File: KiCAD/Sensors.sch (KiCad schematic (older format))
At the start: 15 parts

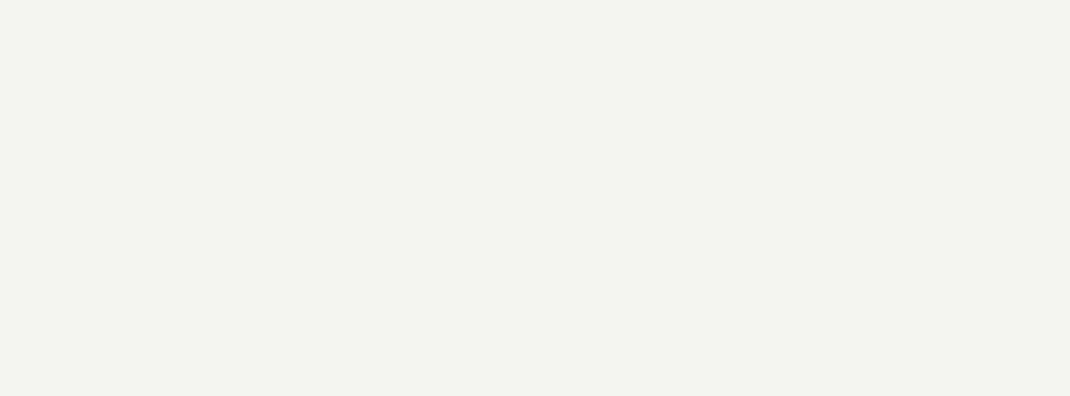
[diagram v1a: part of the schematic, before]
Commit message: Added CAN Bus Sheet
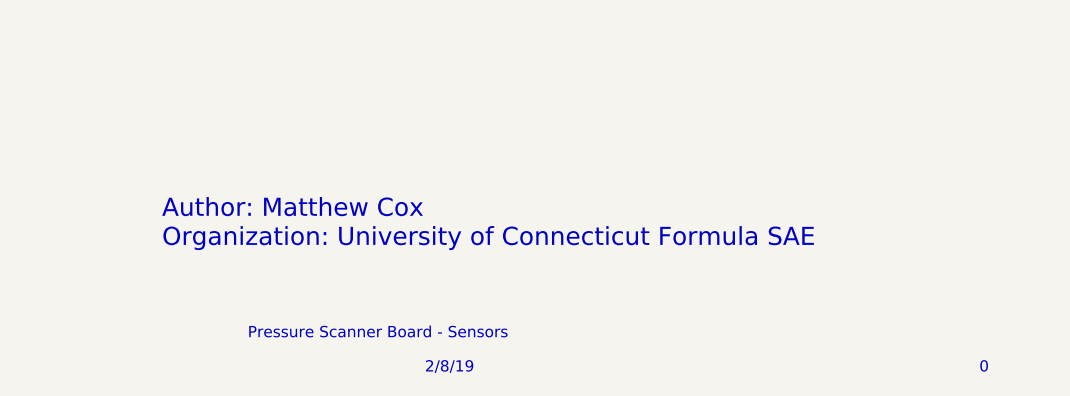
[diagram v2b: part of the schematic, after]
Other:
- note added: "0"
- note added: "2/8/19"
- note added: "Author: Matthew Cox\nOrganization: University of Connecticut Formula SAE"
- note added: "Pressure Scanner Board - Sensors"
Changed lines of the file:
@@
 LIBS:lm1117_edited
 LIBS:MF-MSMF050-2
+LIBS:mcp2515
+LIBS:mcp2551
+LIBS:cesd5v0ap
 LIBS:Pressure Scanner Board-cache
 EELAYER 25 0
@@
 $Descr A4 11693 8268
 encoding utf-8
-Sheet 3 3
+Sheet 3 4
 Title ""
 Date ""
@@
 Wire Notes Line
 	6550 1400 4325 1400
+Text Notes 7375 7500 0    49   ~ 0
+Pressure Scanner Board - Sensors
+Text Notes 8150 7650 0    49   ~ 0
+2/8/19
+Text Notes 10575 7650 0    49   ~ 0
+0
+Text Notes 7000 7100 0    79   ~ 0
+Author: Matthew Cox\nOrganization: University of Connecticut Formula SAE
 $EndSCHEMATC

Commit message: Schematic Rev 0
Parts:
- gave numbers to parts that had none: 15
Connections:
- net EOC_0: no longer names the net of U5.5 (EOC)
- net EOC_1: no longer names the net of U7.5 (EOC)
- net EOC_2: no longer names the net of U9.5 (EOC)
- net EOC_3: no longer names the net of U11.5 (EOC)
- net EOC_4: no longer names the net of U6.5 (EOC)
- net EOC_5: no longer names the net of U8.5 (EOC)
- net EOC_6: no longer names the net of U10.5 (EOC)
- net EOC_7: no longer names the net of U12.5 (EOC)
- no-connect marks 0 -> 8
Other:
- note added: "Low voltage signal -> MCU\nHigh voltage signal -> Sensor"
- moved on the sheet: Q2, Q3, R6, R7, R8, R9

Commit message: Associated sensor footprints with parts
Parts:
- U10, U11, U12, U5, U6, U7, U8, U9: footprint (none) -> DLHR-L10D-E1BD-C-NAV8:DLHR-L10D-E1BD-C-NAV8
- U4: footprint (none) -> HSCDANN015PA2A5:HSCDANN015PA2A5
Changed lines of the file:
@@
 $EndDescr
 $Comp
-L +3.3V #PWR35
+L +3.3V #PWR033
 U 1 1 5C62E178
 P 2175 1700
-F 0 "#PWR35" H 2175 1550 50  0001 C CNN
+F 0 "#PWR033" H 2175 1550 50  0001 C CNN
 F 1 "+3.3V" H 2175 1840 50  0000 C CNN
 F 2 "" H 2175 1700 50  0001 C CNN
@@
 	2175 1900 2525 1900
 $Comp
-L GND #PWR37
+L GND #PWR034
 U 1 1 5C62E1C6
 P 2425 1775
-F 0 "#PWR37" H 2425 1525 50  0001 C CNN
+F 0 "#PWR034" H 2425 1525 50  0001 C CNN
 F 1 "GND" H 2425 1625 50  0000 C CNN
 F 2 "" H 2425 1775 50  0001 C CNN
@@
 F 0 "U5" H 3075 1650 60  0000 C CNN
 F 1 "DLHR-L10D-E1BD-C-NAV8" H 3075 2300 39  0000 C CNN
-F 2 "" H 3075 1975 60  0001 C CNN
+F 2 "DLHR-L10D-E1BD-C-NAV8:DLHR-L10D-E1BD-C-NAV8" H 3075 1975 60  0001 C CNN
 F 3 "" H 3075 1975 60  0001 C CNN
 	1    3075 1975
@@
 	3825 1775 3600 1775
 $Comp
-L +3.3V #PWR43
+L +3.3V #PWR035
 U 1 1 5C62E3C1
 P 2175 2650
-F 0 "#PWR43" H 2175 2500 50  0001 C CNN
+F 0 "#PWR035" H 2175 2500 50  0001 C CNN
 F 1 "+3.3V" H 2175 2790 50  0000 C CNN
 F 2 "" H 2175 2650 50  0001 C CNN
@@
 	2175 2850 2525 2850
 $Comp
-L GND #PWR45
+L GND #PWR036
 U 1 1 5C62E3C9
 P 2425 2725
-F 0 "#PWR45" H 2425 2475 50  0001 C CNN
+F 0 "#PWR036" H 2425 2475 50  0001 C CNN
 F 1 "GND" H 2425 2575 50  0000 C CNN
 F 2 "" H 2425 2725 50  0001 C CNN
@@
 F 0 "U7" H 3075 2600 60  0000 C CNN
 F 1 "DLHR-L10D-E1BD-C-NAV8" H 3075 3250 39  0000 C CNN
-F 2 "" H 3075 2925 60  0001 C CNN
+F 2 "DLHR-L10D-E1BD-C-NAV8:DLHR-L10D-E1BD-C-NAV8" H 3075 2925 60  0001 C CNN
 F 3 "" H 3075 2925 60  0001 C CNN
 	1    3075 2925
@@
 	3825 2725 3600 2725
 $Comp
-L +3.3V #PWR47
+L +3.3V #PWR037
 U 1 1 5C62E42E
 P 2175 3600
-F 0 "#PWR47" H 2175 3450 50  0001 C CNN
+F 0 "#PWR037" H 2175 3450 50  0001 C CNN
 F 1 "+3.3V" H 2175 3740 50  0000 C CNN
 F 2 "" H 2175 3600 50  0001 C CNN
@@
 	2175 3800 2525 3800
 $Comp
-L GND #PWR49
+L GND #PWR038
 U 1 1 5C62E436
 P 2425 3675
-F 0 "#PWR49" H 2425 3425 50  0001 C CNN
+F 0 "#PWR038" H 2425 3425 50  0001 C CNN
 F 1 "GND" H 2425 3525 50  0000 C CNN
 F 2 "" H 2425 3675 50  0001 C CNN
@@
 F 0 "U9" H 3075 3550 60  0000 C CNN
 F 1 "DLHR-L10D-E1BD-C-NAV8" H 3075 4200 39  0000 C CNN
-F 2 "" H 3075 3875 60  0001 C CNN
+F 2 "DLHR-L10D-E1BD-C-NAV8:DLHR-L10D-E1BD-C-NAV8" H 3075 3875 60  0001 C CNN
 F 3 "" H 3075 3875 60  0001 C CNN
 	1    3075 3875
@@
 	3825 3675 3600 3675
 $Comp
-L +3.3V #PWR51
+L +3.3V #PWR039
 U 1 1 5C62E4AC
 P 2175 4575
-F 0 "#PWR51" H 2175 4425 50  0001 C CNN
+F 0 "#PWR039" H 2175 4425 50  0001 C CNN
 F 1 "+3.3V" H 2175 4715 50  0000 C CNN
 F 2 "" H 2175 4575 50  0001 C CNN
@@
 	2175 4775 2525 4775
 $Comp
-L GND #PWR53
+L GND #PWR040
 U 1 1 5C62E4B4
 P 2425 4650
-F 0 "#PWR53" H 2425 4400 50  0001 C CNN
+F 0 "#PWR040" H 2425 4400 50  0001 C CNN
 F 1 "GND" H 2425 4500 50  0000 C CNN
 F 2 "" H 2425 4650 50  0001 C CNN
@@
 F 0 "U11" H 3075 4525 60  0000 C CNN
 F 1 "DLHR-L10D-E1BD-C-NAV8" H 3075 5175 39  0000 C CNN
-F 2 "" H 3075 4850 60  0001 C CNN
+F 2 "DLHR-L10D-E1BD-C-NAV8:DLHR-L10D-E1BD-C-NAV8" H 3075 4850 60  0001 C CNN
 F 3 "" H 3075 4850 60  0001 C CNN
 	1    3075 4850
@@
 	3825 4650 3600 4650
 $Comp
-L +3.3V #PWR36
+L +3.3V #PWR041
 U 1 1 5C62E67B
 P 4500 1700
-F 0 "#PWR36" H 4500 1550 50  0001 C CNN
+F 0 "#PWR041" H 4500 1550 50  0001 C CNN
 F 1 "+3.3V" H 4500 1840 50  0000 C CNN
 F 2 "" H 4500 1700 50  0001 C CNN
@@
 	4500 1900 4850 1900
 $Comp
-L GND #PWR38
+L GND #PWR042
 U 1 1 5C62E683
 P 4750 1775
-F 0 "#PWR38" H 4750 1525 50  0001 C CNN
+F 0 "#PWR042" H 4750 1525 50  0001 C CNN
 F 1 "GND" H 4750 1625 50  0000 C CNN
 F 2 "" H 4750 1775 50  0001 C CNN
@@
 F 0 "U6" H 5400 1650 60  0000 C CNN
 F 1 "DLHR-L10D-E1BD-C-NAV8" H 5400 2300 39  0000 C CNN
-F 2 "" H 5400 1975 60  0001 C CNN
+F 2 "DLHR-L10D-E1BD-C-NAV8:DLHR-L10D-E1BD-C-NAV8" H 5400 1975 60  0001 C CNN
 F 3 "" H 5400 1975 60  0001 C CNN
 	1    5400 1975
@@
 	6150 1775 5925 1775
 $Comp
-L +3.3V #PWR44
+L +3.3V #PWR043
 U 1 1 5C62E69A
 P 4500 2650
-F 0 "#PWR44" H 4500 2500 50  0001 C CNN
+F 0 "#PWR043" H 4500 2500 50  0001 C CNN
 F 1 "+3.3V" H 4500 2790 50  0000 C CNN
 F 2 "" H 4500 2650 50  0001 C CNN
@@
 	4500 2850 4850 2850
 $Comp
-L GND #PWR46
+L GND #PWR044
 U 1 1 5C62E6A2
 P 4750 2725
-F 0 "#PWR46" H 4750 2475 50  0001 C CNN
+F 0 "#PWR044" H 4750 2475 50  0001 C CNN
 F 1 "GND" H 4750 2575 50  0000 C CNN
 F 2 "" H 4750 2725 50  0001 C CNN
@@
 F 0 "U8" H 5400 2600 60  0000 C CNN
 F 1 "DLHR-L10D-E1BD-C-NAV8" H 5400 3250 39  0000 C CNN
-F 2 "" H 5400 2925 60  0001 C CNN
+F 2 "DLHR-L10D-E1BD-C-NAV8:DLHR-L10D-E1BD-C-NAV8" H 5400 2925 60  0001 C CNN
 F 3 "" H 5400 2925 60  0001 C CNN
 	1    5400 2925
@@
 	6150 2725 5925 2725
 $Comp
-L +3.3V #PWR48
+L +3.3V #PWR045
 U 1 1 5C62E6B9
 P 4500 3600
-F 0 "#PWR48" H 4500 3450 50  0001 C CNN
+F 0 "#PWR045" H 4500 3450 50  0001 C CNN
 F 1 "+3.3V" H 4500 3740 50  0000 C CNN
 F 2 "" H 4500 3600 50  0001 C CNN
@@
 	4500 3800 4850 3800
 $Comp
-L GND #PWR50
+L GND #PWR046
 U 1 1 5C62E6C1
 P 4750 3675
-F 0 "#PWR50" H 4750 3425 50  0001 C CNN
+F 0 "#PWR046" H 4750 3425 50  0001 C CNN
 F 1 "GND" H 4750 3525 50  0000 C CNN
 F 2 "" H 4750 3675 50  0001 C CNN
@@
 F 0 "U10" H 5400 3550 60  0000 C CNN
 F 1 "DLHR-L10D-E1BD-C-NAV8" H 5400 4200 39  0000 C CNN
-F 2 "" H 5400 3875 60  0001 C CNN
+F 2 "DLHR-L10D-E1BD-C-NAV8:DLHR-L10D-E1BD-C-NAV8" H 5400 3875 60  0001 C CNN
 F 3 "" H 5400 3875 60  0001 C CNN
 	1    5400 3875
@@
 	6150 3675 5925 3675
 $Comp
-L +3.3V #PWR52
+L +3.3V #PWR047
 U 1 1 5C62E6D8
 P 4500 4575
-F 0 "#PWR52" H 4500 4425 50  0001 C CNN
+F 0 "#PWR047" H 4500 4425 50  0001 C CNN
 F 1 "+3.3V" H 4500 4715 50  0000 C CNN
 F 2 "" H 4500 4575 50  0001 C CNN
@@
 	4500 4775 4850 4775
 $Comp
-L GND #PWR54
+L GND #PWR048
 U 1 1 5C62E6E0
 P 4750 4650
-F 0 "#PWR54" H 4750 4400 50  0001 C CNN
+F 0 "#PWR048" H 4750 4400 50  0001 C CNN
 F 1 "GND" H 4750 4500 50  0000 C CNN
 F 2 "" H 4750 4650 50  0001 C CNN
@@
 F 0 "U12" H 5400 4525 60  0000 C CNN
 F 1 "DLHR-L10D-E1BD-C-NAV8" H 5400 5175 39  0000 C CNN
-F 2 "" H 5400 4850 60  0001 C CNN
+F 2 "DLHR-L10D-E1BD-C-NAV8:DLHR-L10D-E1BD-C-NAV8" H 5400 4850 60  0001 C CNN
 F 3 "" H 5400 4850 60  0001 C CNN
 	1    5400 4850
@@
 F 0 "U4" H 9175 1625 39  0000 C CNN
 F 1 "HSCDANN015PA2A5" H 9175 2100 39  0000 C CNN
-F 2 "" H 9175 1825 59  0001 C CNN
+F 2 "HSCDANN015PA2A5:HSCDANN015PA2A5" H 9175 1825 59  0001 C CNN
 F 3 "" H 9175 1825 59  0001 C CNN
 	1    9175 1825
@@
 $EndComp
 $Comp
-L GND #PWR34
+L GND #PWR049
 U 1 1 5C62EFEF
 P 8625 1675
-F 0 "#PWR34" H 8625 1425 50  0001 C CNN
+F 0 "#PWR049" H 8625 1425 50  0001 C CNN
 F 1 "GND" H 8625 1525 50  0000 C CNN
 F 2 "" H 8625 1675 50  0001 C CNN
@@
 	8625 1675 8725 1675
 $Comp
-L +5V #PWR33
+L +5V #PWR050
 U 1 1 5C62F065
 P 8250 1675
-F 0 "#PWR33" H 8250 1525 50  0001 C CNN
+F 0 "#PWR050" H 8250 1525 50  0001 C CNN
 F 1 "+5V" H 8250 1815 50  0000 C CNN
 F 2 "" H 8250 1675 50  0001 C CNN
@@
 	8500 2625 8500 2825
 $Comp
-L +3.3V #PWR39
+L +3.3V #PWR051
 U 1 1 5C62FBAB
 P 8225 2575
-F 0 "#PWR39" H 8225 2425 50  0001 C CNN
+F 0 "#PWR051" H 8225 2425 50  0001 C CNN
 F 1 "+3.3V" H 8225 2715 50  0000 C CNN
 F 2 "" H 8225 2575 50  0001 C CNN
@@
 Connection ~ 8800 3125
 $Comp
-L +5V #PWR40
+L +5V #PWR052
 U 1 1 5C62FE33
 P 8800 2575
-F 0 "#PWR40" H 8800 2425 50  0001 C CNN
+F 0 "#PWR052" H 8800 2425 50  0001 C CNN
 F 1 "+5V" H 8800 2715 50  0000 C CNN
 F 2 "" H 8800 2575 50  0001 C CNN
@@
 	9850 2625 9850 2825
 $Comp
-L +3.3V #PWR41
+L +3.3V #PWR053
 U 1 1 5C630157
 P 9575 2575
-F 0 "#PWR41" H 9575 2425 50  0001 C CNN
+F 0 "#PWR053" H 9575 2425 50  0001 C CNN
 F 1 "+3.3V" H 9575 2715 50  0000 C CNN
 F 2 "" H 9575 2575 50  0001 C CNN
@@
 Connection ~ 10150 3125
 $Comp
-L +5V #PWR42
+L +5V #PWR054
 U 1 1 5C630167
 P 10150 2575
-F 0 "#PWR42" H 10150 2425 50  0001 C CNN
+F 0 "#PWR054" H 10150 2425 50  0001 C CNN
 F 1 "+5V" H 10150 2715 50  0000 C CNN
 F 2 "" H 10150 2575 50  0001 C CNN

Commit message: Added footprints for all components and created BOM
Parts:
- Q2, Q3: footprint (none) -> TO_SOT_Packages_SMD:SOT-23
- R6, R7, R8, R9: footprint (none) -> Resistors_SMD:R_1210
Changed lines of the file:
@@
 $EndDescr
 $Comp
-L +3.3V #PWR033
+L +3.3V #PWR031
 U 1 1 5C62E178
 P 2175 1700
-F 0 "#PWR033" H 2175 1550 50  0001 C CNN
+F 0 "#PWR031" H 2175 1550 50  0001 C CNN
 F 1 "+3.3V" H 2175 1840 50  0000 C CNN
 F 2 "" H 2175 1700 50  0001 C CNN
@@
 	2175 1900 2525 1900
 $Comp
-L GND #PWR034
+L GND #PWR032
 U 1 1 5C62E1C6
 P 2425 1775
-F 0 "#PWR034" H 2425 1525 50  0001 C CNN
+F 0 "#PWR032" H 2425 1525 50  0001 C CNN
 F 1 "GND" H 2425 1625 50  0000 C CNN
 F 2 "" H 2425 1775 50  0001 C CNN
@@
 	3825 1775 3600 1775
 $Comp
-L +3.3V #PWR035
+L +3.3V #PWR033
 U 1 1 5C62E3C1
 P 2175 2650
-F 0 "#PWR035" H 2175 2500 50  0001 C CNN
+F 0 "#PWR033" H 2175 2500 50  0001 C CNN
 F 1 "+3.3V" H 2175 2790 50  0000 C CNN
 F 2 "" H 2175 2650 50  0001 C CNN
@@
 	2175 2850 2525 2850
 $Comp
-L GND #PWR036
+L GND #PWR034
 U 1 1 5C62E3C9
 P 2425 2725
-F 0 "#PWR036" H 2425 2475 50  0001 C CNN
+F 0 "#PWR034" H 2425 2475 50  0001 C CNN
 F 1 "GND" H 2425 2575 50  0000 C CNN
 F 2 "" H 2425 2725 50  0001 C CNN
@@
 	3825 2725 3600 2725
 $Comp
-L +3.3V #PWR037
+L +3.3V #PWR035
 U 1 1 5C62E42E
 P 2175 3600
-F 0 "#PWR037" H 2175 3450 50  0001 C CNN
+F 0 "#PWR035" H 2175 3450 50  0001 C CNN
 F 1 "+3.3V" H 2175 3740 50  0000 C CNN
 F 2 "" H 2175 3600 50  0001 C CNN
@@
 	2175 3800 2525 3800
 $Comp
-L GND #PWR038
+L GND #PWR036
 U 1 1 5C62E436
 P 2425 3675
-F 0 "#PWR038" H 2425 3425 50  0001 C CNN
+F 0 "#PWR036" H 2425 3425 50  0001 C CNN
 F 1 "GND" H 2425 3525 50  0000 C CNN
 F 2 "" H 2425 3675 50  0001 C CNN
@@
 	3825 3675 3600 3675
 $Comp
-L +3.3V #PWR039
+L +3.3V #PWR037
 U 1 1 5C62E4AC
 P 2175 4575
-F 0 "#PWR039" H 2175 4425 50  0001 C CNN
+F 0 "#PWR037" H 2175 4425 50  0001 C CNN
 F 1 "+3.3V" H 2175 4715 50  0000 C CNN
 F 2 "" H 2175 4575 50  0001 C CNN
@@
 	2175 4775 2525 4775
 $Comp
-L GND #PWR040
+L GND #PWR038
 U 1 1 5C62E4B4
 P 2425 4650
-F 0 "#PWR040" H 2425 4400 50  0001 C CNN
+F 0 "#PWR038" H 2425 4400 50  0001 C CNN
 F 1 "GND" H 2425 4500 50  0000 C CNN
 F 2 "" H 2425 4650 50  0001 C CNN
@@
 	3825 4650 3600 4650
 $Comp
-L +3.3V #PWR041
+L +3.3V #PWR039
 U 1 1 5C62E67B
 P 4500 1700
-F 0 "#PWR041" H 4500 1550 50  0001 C CNN
+F 0 "#PWR039" H 4500 1550 50  0001 C CNN
 F 1 "+3.3V" H 4500 1840 50  0000 C CNN
 F 2 "" H 4500 1700 50  0001 C CNN
@@
 	4500 1900 4850 1900
 $Comp
-L GND #PWR042
+L GND #PWR040
 U 1 1 5C62E683
 P 4750 1775
-F 0 "#PWR042" H 4750 1525 50  0001 C CNN
+F 0 "#PWR040" H 4750 1525 50  0001 C CNN
 F 1 "GND" H 4750 1625 50  0000 C CNN
 F 2 "" H 4750 1775 50  0001 C CNN
@@
 	6150 1775 5925 1775
 $Comp
-L +3.3V #PWR043
+L +3.3V #PWR041
 U 1 1 5C62E69A
 P 4500 2650
-F 0 "#PWR043" H 4500 2500 50  0001 C CNN
+F 0 "#PWR041" H 4500 2500 50  0001 C CNN
 F 1 "+3.3V" H 4500 2790 50  0000 C CNN
 F 2 "" H 4500 2650 50  0001 C CNN
@@
 	4500 2850 4850 2850
 $Comp
-L GND #PWR044
+L GND #PWR042
 U 1 1 5C62E6A2
 P 4750 2725
-F 0 "#PWR044" H 4750 2475 50  0001 C CNN
+F 0 "#PWR042" H 4750 2475 50  0001 C CNN
 F 1 "GND" H 4750 2575 50  0000 C CNN
 F 2 "" H 4750 2725 50  0001 C CNN
@@
 	6150 2725 5925 2725
 $Comp
-L +3.3V #PWR045
+L +3.3V #PWR043
 U 1 1 5C62E6B9
 P 4500 3600
-F 0 "#PWR045" H 4500 3450 50  0001 C CNN
+F 0 "#PWR043" H 4500 3450 50  0001 C CNN
 F 1 "+3.3V" H 4500 3740 50  0000 C CNN
 F 2 "" H 4500 3600 50  0001 C CNN
@@
 	4500 3800 4850 3800
 $Comp
-L GND #PWR046
+L GND #PWR044
 U 1 1 5C62E6C1
 P 4750 3675
-F 0 "#PWR046" H 4750 3425 50  0001 C CNN
+F 0 "#PWR044" H 4750 3425 50  0001 C CNN
 F 1 "GND" H 4750 3525 50  0000 C CNN
 F 2 "" H 4750 3675 50  0001 C CNN
@@
 	6150 3675 5925 3675
 $Comp
-L +3.3V #PWR047
+L +3.3V #PWR045
 U 1 1 5C62E6D8
 P 4500 4575
-F 0 "#PWR047" H 4500 4425 50  0001 C CNN
+F 0 "#PWR045" H 4500 4425 50  0001 C CNN
 F 1 "+3.3V" H 4500 4715 50  0000 C CNN
 F 2 "" H 4500 4575 50  0001 C CNN
@@
 	4500 4775 4850 4775
 $Comp
-L GND #PWR048
+L GND #PWR046
 U 1 1 5C62E6E0
 P 4750 4650
-F 0 "#PWR048" H 4750 4400 50  0001 C CNN
+F 0 "#PWR046" H 4750 4400 50  0001 C CNN
 F 1 "GND" H 4750 4500 50  0000 C CNN
 F 2 "" H 4750 4650 50  0001 C CNN
@@
 $EndComp
 $Comp
-L GND #PWR049
+L GND #PWR047
 U 1 1 5C62EFEF
 P 8625 1675
-F 0 "#PWR049" H 8625 1425 50  0001 C CNN
+F 0 "#PWR047" H 8625 1425 50  0001 C CNN
 F 1 "GND" H 8625 1525 50  0000 C CNN
 F 2 "" H 8625 1675 50  0001 C CNN
@@
 	8625 1675 8725 1675
 $Comp
-L +5V #PWR050
+L +5V #PWR048
 U 1 1 5C62F065
 P 8250 1675
-F 0 "#PWR050" H 8250 1525 50  0001 C CNN
+F 0 "#PWR048" H 8250 1525 50  0001 C CNN
 F 1 "+5V" H 8250 1815 50  0000 C CNN
 F 2 "" H 8250 1675 50  0001 C CNN
@@
 F 0 "Q2" V 8750 2925 50  0000 L CNN
 F 1 "BSS138" V 8825 2925 50  0000 L CNN
-F 2 "" H 8700 3125 50  0001 C CNN
+F 2 "TO_SOT_Packages_SMD:SOT-23" H 8700 3125 50  0001 C CNN
 F 3 "" H 8500 3025 50  0001 C CNN
 	1    8500 3025
@@
 F 0 "R6" V 8305 2850 50  0000 C CNN
 F 1 "10K" V 8225 2850 50  0000 C CNN
-F 2 "" V 8155 2850 50  0001 C CNN
+F 2 "Resistors_SMD:R_1210" V 8155 2850 50  0001 C CNN
 F 3 "" H 8225 2850 50  0001 C CNN
 	1    8225 2850
@@
 	8500 2625 8500 2825
 $Comp
-L +3.3V #PWR051
+L +3.3V #PWR049
 U 1 1 5C62FBAB
 P 8225 2575
-F 0 "#PWR051" H 8225 2425 50  0001 C CNN
+F 0 "#PWR049" H 8225 2425 50  0001 C CNN
 F 1 "+3.3V" H 8225 2715 50  0000 C CNN
 F 2 "" H 8225 2575 50  0001 C CNN
@@
 F 0 "R7" V 8880 2850 50  0000 C CNN
 F 1 "10K" V 8800 2850 50  0000 C CNN
-F 2 "" V 8730 2850 50  0001 C CNN
+F 2 "Resistors_SMD:R_1210" V 8730 2850 50  0001 C CNN
 F 3 "" H 8800 2850 50  0001 C CNN
 	1    8800 2850
@@
 Connection ~ 8800 3125
 $Comp
-L +5V #PWR052
+L +5V #PWR050
 U 1 1 5C62FE33
 P 8800 2575
-F 0 "#PWR052" H 8800 2425 50  0001 C CNN
+F 0 "#PWR050" H 8800 2425 50  0001 C CNN
 F 1 "+5V" H 8800 2715 50  0000 C CNN
 F 2 "" H 8800 2575 50  0001 C CNN
@@
 F 0 "Q3" V 10100 2925 50  0000 L CNN
 F 1 "BSS138" V 10175 2925 50  0000 L CNN
-F 2 "" H 10050 3125 50  0001 C CNN
+F 2 "TO_SOT_Packages_SMD:SOT-23" H 10050 3125 50  0001 C CNN
 F 3 "" H 9850 3025 50  0001 C CNN
 	1    9850 3025
@@
 F 0 "R8" V 9655 2850 50  0000 C CNN
 F 1 "10K" V 9575 2850 50  0000 C CNN
-F 2 "" V 9505 2850 50  0001 C CNN
+F 2 "Resistors_SMD:R_1210" V 9505 2850 50  0001 C CNN
 F 3 "" H 9575 2850 50  0001 C CNN
 	1    9575 2850
@@
 	9850 2625 9850 2825
 $Comp
-L +3.3V #PWR053
+L +3.3V #PWR051
 U 1 1 5C630157
 P 9575 2575
-F 0 "#PWR053" H 9575 2425 50  0001 C CNN
+F 0 "#PWR051" H 9575 2425 50  0001 C CNN
 F 1 "+3.3V" H 9575 2715 50  0000 C CNN
 F 2 "" H 9575 2575 50  0001 C CNN
@@
 F 0 "R9" V 10230 2850 50  0000 C CNN
 F 1 "10K" V 10150 2850 50  0000 C CNN
-F 2 "" V 10080 2850 50  0001 C CNN
+F 2 "Resistors_SMD:R_1210" V 10080 2850 50  0001 C CNN
 F 3 "" H 10150 2850 50  0001 C CNN
 	1    10150 2850
@@
 Connection ~ 10150 3125
 $Comp
-L +5V #PWR054
+L +5V #PWR052
 U 1 1 5C630167
 P 10150 2575
-F 0 "#PWR054" H 10150 2425 50  0001 C CNN
+F 0 "#PWR052" H 10150 2425 50  0001 C CNN
 F 1 "+5V" H 10150 2715 50  0000 C CNN
 F 2 "" H 10150 2575 50  0001 C CNN

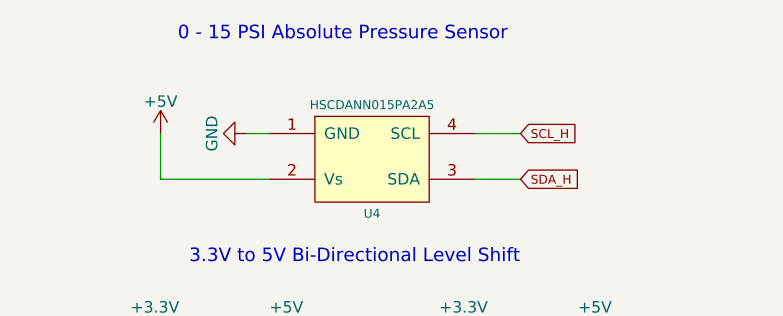
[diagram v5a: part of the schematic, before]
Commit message: Corrected schematic error, began layout.
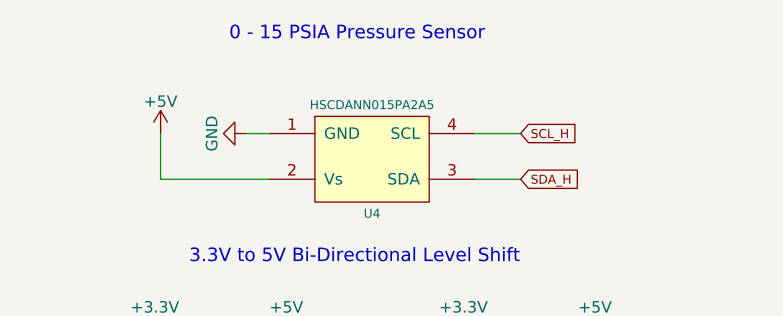
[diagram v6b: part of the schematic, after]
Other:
- note added: "0 - 15 PSIA Pressure Sensor"
- note removed: "0 - 15 PSI Absolute Pressure Sensor"
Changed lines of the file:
@@
 Text Notes 4875 5525 0    59   ~ 0
 Optional Expansion Slots
-Text Notes 8325 1275 0    59   ~ 0
-0 - 15 PSI Absolute Pressure Sensor
+Text Notes 8550 1275 0    59   ~ 0
+0 - 15 PSIA Pressure Sensor
 $Comp
 L HSCDANN015PA2A5 U4
